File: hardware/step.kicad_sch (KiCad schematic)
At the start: 51 parts, among them J101 WAGO 2065-100, J102 WAGO 2065-100, J103 Cortex, SW101 SKSG, SW102 SKSG, U101 ATSAMD51J, U102 TPS78433QWDRBRQ1, Y101 32k768

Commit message: Refresh
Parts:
- C107, C108: Manufacturer YAGEO -> TDK; Mouser 603-CC603JRNPO9BN180 -> 810-CGA3E2C0G1H180J; Product CC0603JRNPO9BN180 -> CGA3E2C0G1H180J080AA
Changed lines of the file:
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@@
 	(title_block
 		(title "V2 step")
-		(date "2026-03-02")
+		(date "2026-03-11")
 		(rev "2025-11-30")
 		(company "Versio Duo")
@@
 			)
 		)
-		(property "Description" "Unpolarized capacitor, small symbol"
+		(property "Description" ""
 			(at 109.22 37.592 0)
 			(effects
@@
 		(at 223.52 165.1 0)
 		(unit 1)
-		(exclude_from_sim yes)
+		(exclude_from_sim no)
 		(in_bom no)
 		(on_board yes)
@@
 			)
 		)
+		(property "Sim.Enable" "0"
+			(at 223.52 165.1 0)
+			(effects
+				(font
+					(size 1.27 1.27)
+				)
+				(hide yes)
+			)
+		)
 		(instances
 			(project ""
@@
 			)
 		)
-		(property "Description" "Push button switch, generic, two pins"
+		(property "Description" "Push button"
 			(at 118.11 157.48 0)
 			(effects
@@
 			)
 		)
-		(property "Description" "Light emitting diode, small symbol"
+		(property "Description" ""
 			(at 128.27 86.36 0)
 			(effects
@@
 			)
 		)
-		(property "Description" "Resistor, small symbol"
+		(property "Description" ""
 			(at 243.84 80.772 0)
 			(effects
@@
 		(at 190.5 152.4 0)
 		(unit 1)
-		(exclude_from_sim yes)
+		(exclude_from_sim no)
 		(in_bom no)
 		(on_board yes)
@@
 			)
 		)
+		(property "Sim.Enable" "0"
+			(at 190.5 152.4 0)
+			(effects
+				(font
+					(size 1.27 1.27)
+				)
+				(hide yes)
+			)
+		)
 		(instances
 			(project "pulse"
@@
 			)
 		)
-		(property "Description" "Unpolarized capacitor, small symbol"
+		(property "Description" ""
 			(at 58.42 182.372 0)
 			(effects
@@
 		(at 223.52 152.4 0)
 		(unit 1)
-		(exclude_from_sim yes)
+		(exclude_from_sim no)
 		(in_bom no)
 		(on_board yes)
@@
 			)
 		)
+		(property "Sim.Enable" "0"
+			(at 223.52 152.4 0)
+			(effects
+				(font
+					(size 1.27 1.27)
+				)
+				(hide yes)
+			)
+		)
 		(instances
 			(project "pulse"
@@
 			)
 		)
-		(property "Description" "Unpolarized capacitor, small symbol"
+		(property "Description" ""
 			(at 119.38 37.592 0)
 			(effects
@@
 			)
 		)
-		(property "Description" "Resistor, small symbol"
+		(property "Description" ""
 			(at 268.732 66.04 0)
 			(effects
@@
 		(at 190.5 160.02 0)
 		(unit 1)
-		(exclude_from_sim yes)
+		(exclude_from_sim no)
 		(in_bom no)
 		(on_board yes)
@@
 			)
 		)
+		(property "Sim.Enable" "0"
+			(at 190.5 160.02 0)
+			(effects
+				(font
+					(size 1.27 1.27)
+				)
+				(hide yes)
+			)
+		)
 		(instances
 			(project "pulse"
@@
 			)
 		)
-		(property "Description" "Unpolarized capacitor, small symbol"
+		(property "Description" ""
 			(at 33.02 182.372 0)
 			(effects
@@
 			)
 		)
-		(property "Description" "Two pin crystal, small symbol"
+		(property "Description" ""
 			(at 24.13 43.18 0)
 			(effects
@@
 			)
 		)
-		(property "Description" "Unpolarized capacitor, small symbol"
+		(property "Description" ""
 			(at 26.67 60.452 0)
 			(effects
@@
 			)
 		)
-		(property "Mouser" "603-CC603JRNPO9BN180"
+		(property "Mouser" "810-CGA3E2C0G1H180J"
 			(at 26.67 64.516 0)
 			(effects
@@
 			)
 		)
-		(property "Product" "CC0603JRNPO9BN180"
+		(property "Product" "CGA3E2C0G1H180J080AA"
 			(at 26.67 67.564 0)
 			(effects
@@
 			)
 		)
-		(property "Manufacturer" "YAGEO"
+		(property "Manufacturer" "TDK"
 			(at 26.67 64.77 0)
 			(effects
@@
 			)
 		)
-		(property "Description" "Unpolarized capacitor, small symbol"
+		(property "Description" ""
 			(at 57.15 37.592 0)
 			(effects
@@
 			)
 		)
-		(property "Description" "Unpolarized capacitor, small symbol"
+		(property "Description" ""
 			(at 21.59 60.452 0)
 			(effects
@@
 			)
 		)
-		(property "Mouser" "603-CC603JRNPO9BN180"
+		(property "Mouser" "810-CGA3E2C0G1H180J"
 			(at 21.59 64.516 0)
 			(effects
@@
 			)
 		)
-		(property "Product" "CC0603JRNPO9BN180"
+		(property "Product" "CGA3E2C0G1H180J080AA"
 			(at 21.59 67.564 0)
 			(effects
@@
 			)
 		)
-		(property "Manufacturer" "YAGEO"
+		(property "Manufacturer" "TDK"
 			(at 21.59 64.77 0)
 			(effects
@@
 		(at 157.48 160.02 0)
 		(unit 1)
-		(exclude_from_sim yes)
+		(exclude_from_sim no)
 		(in_bom no)
 		(on_board yes)
@@
 			)
 		)
+		(property "Sim.Enable" "0"
+			(at 157.48 160.02 0)
+			(effects
+				(font
+					(size 1.27 1.27)
+				)
+				(hide yes)
+			)
+		)
 		(instances
 			(project ""
@@
 			)
 		)
-		(property "Description" "Resistor, small symbol"
+		(property "Description" ""
 			(at 149.352 86.36 0)
 			(effects
@@
 			)
 		)
-		(property "Description" "Unpolarized capacitor, small symbol"
+		(property "Description" ""
 			(at 261.62 82.042 0)
 			(effects
@@
 			)
 		)
-		(property "Description" "Unpolarized capacitor, small symbol"
+		(property "Description" ""
 			(at 99.06 37.592 0)
 			(effects
@@
 			)
 		)
-		(property "Description" "Unpolarized capacitor, small symbol"
+		(property "Description" ""
 			(at 78.74 37.592 0)
 			(effects
@@
 		(at 223.52 158.75 0)
 		(unit 1)
-		(exclude_from_sim yes)
+		(exclude_from_sim no)
 		(in_bom no)
 		(on_board yes)
@@
 			)
 		)
+		(property "Sim.Enable" "0"
+			(at 223.52 158.75 0)
+			(effects
+				(font
+					(size 1.27 1.27)
+				)
+				(hide yes)
+			)
+		)
 		(instances
 			(project ""
@@
 			)
 		)
-		(property "Description" "Push button switch, generic, two pins"
+		(property "Description" "Push button"
 			(at 129.54 73.152 0)
 			(effects
@@
 			)
 		)
-		(property "Description" "Unpolarized capacitor, small symbol"
+		(property "Description" ""
 			(at 88.9 37.592 0)
 			(effects
@@
 			)
 		)
-		(property "Description" "Resistor, small symbol"
+		(property "Description" ""
 			(at 243.84 75.692 0)
 			(effects
@@
 			)
 		)
-		(property "Description" "Resistor, small symbol"
+		(property "Description" ""
 			(at 62.992 121.92 0)
 			(effects
@@
 		(at 190.5 168.91 0)
 		(unit 1)
-		(exclude_from_sim yes)
+		(exclude_from_sim no)
 		(in_bom no)
 		(on_board yes)
@@
 			(at 190.5 168.91 0)
 			(effects
+				(font
+					(size 1.27 1.27)
+				)
+				(hide yes)
+			)
+		)
+		(property "Sim.Enable" "0"
+			(at 190.5 168.91 0)
+			(effects

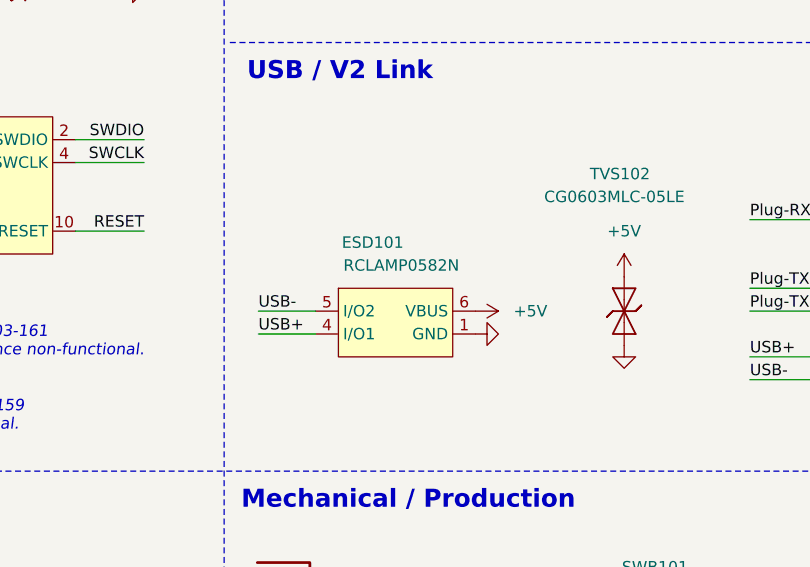
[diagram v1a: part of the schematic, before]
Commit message: Update ESD suppressor
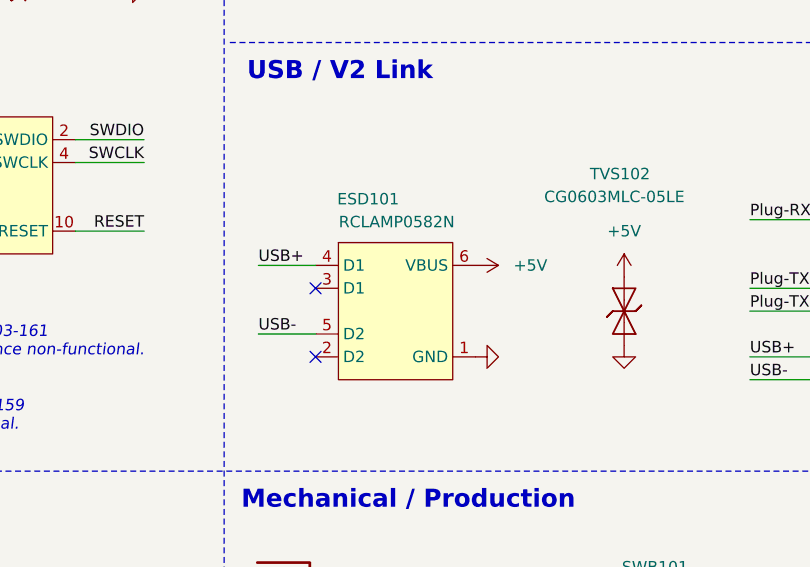
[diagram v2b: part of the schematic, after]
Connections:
- no-connect marks 23 -> 25
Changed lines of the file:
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@@
 	(title_block
 		(title "V2 step")
-		(date "2026-03-11")
+		(date "2026-03-14")
 		(rev "2025-11-30")
 		(company "Versio Duo")
@@
 	)
 	(no_connect
+		(at 161.29 127)
+	)
+	(no_connect
 		(at 133.35 180.34)
 	)
 	(no_connect
+		(at 161.29 119.38)
+	)
+	(no_connect
 		(at 53.34 55.88)
 	)
@@
 	(wire
 		(pts
+			(xy 154.94 116.84) (xy 161.29 116.84)
+		)
+		(stroke
+			(width 0)
+			(type default)
+		)
+	)
+	(wire
+		(pts
 			(xy 72.39 21.59) (xy 72.39 33.02)
 		)
@@
 	(wire
 		(pts
-			(xy 154.94 124.46) (xy 161.29 124.46)
-		)
-		(stroke
-			(width 0)
-			(type default)
-		)
-	)
-	(wire
-		(pts
 			(xy 118.11 173.99) (xy 133.35 173.99)
 		)
@@
 	(wire
 		(pts
-			(xy 154.94 121.92) (xy 161.29 121.92)
+			(xy 154.94 124.46) (xy 161.29 124.46)
 		)
 		(stroke
@@
 		)
 	)
+	(label "USB+"
+		(at 154.94 116.84 0)
+		(effects
+			(font
+				(size 1.27 1.27)
+			)
+			(justify left bottom)
+		)
+	)
 	(label "LED1"
 		(at 160.02 48.26 0)
@@
 	)
 	(label "USB-"
-		(at 154.94 121.92 0)
+		(at 154.94 124.46 0)
 		(effects
 			(font
@@
 		)
 	)
-	(label "USB+"
-		(at 154.94 124.46 0)
-		(effects
-			(font
-				(size 1.27 1.27)
-			)
-			(justify left bottom)
-		)
-	)
 	(label "Socket-TX"
 		(at 247.65 123.19 0)
@@
 	(symbol
 		(lib_id "V2_power:+5V")
-		(at 179.07 121.92 270)
+		(at 179.07 116.84 270)
 		(unit 1)
 		(exclude_from_sim no)
@@
 		(dnp no)
 		(property "Reference" "#PWR124"
-			(at 175.26 121.92 0)
+			(at 175.26 116.84 0)
 			(effects
 				(font
@@
 		)
 		(property "Value" "+5V"
-			(at 185.166 121.92 90)
+			(at 185.166 116.84 90)
 			(effects
 				(font
@@
 		)
 		(property "Footprint" ""
-			(at 179.07 121.92 0)
+			(at 179.07 116.84 0)
 			(effects
 				(font
@@
 		)
 		(property "Datasheet" ""
-			(at 179.07 121.92 0)
+			(at 179.07 116.84 0)
 			(effects
 				(font
@@
 		)
 		(property "Description" ""
-			(at 179.07 121.92 0)
+			(at 179.07 116.84 0)
 			(effects
 				(font
@@
 		(dnp no)
 		(property "Reference" "ESD101"
-			(at 167.64 114.3 0)
+			(at 167.132 109.474 0)
 			(effects
 				(font
@@
 		)
 		(property "Value" "RCLAMP0582N"
-			(at 170.815 116.84 0)
+			(at 170.307 112.014 0)
 			(effects
 				(font
@@
 	(symbol
 		(lib_id "V2_power:GND")
-		(at 179.07 124.46 90)
+		(at 179.07 127 90)
 		(unit 1)
 		(exclude_from_sim no)
@@
 		(dnp no)
 		(property "Reference" "#PWR125"
-			(at 185.42 124.46 0)
+			(at 185.42 127 0)
 			(effects
 				(font
@@
 		)
 		(property "Value" "GND"
-			(at 184.15 124.46 90)
+			(at 184.15 127 90)
 			(effects
 				(font
@@
 		)
 		(property "Footprint" ""
-			(at 179.07 124.46 0)
+			(at 179.07 127 0)
 			(effects
 				(font
@@
 		)
 		(property "Datasheet" ""
-			(at 179.07 124.46 0)
+			(at 179.07 127 0)
 			(effects
 				(font
@@
 		)
 		(property "Description" ""
-			(at 179.07 124.46 0)
+			(at 179.07 127 0)
 			(effects
 				(font

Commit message: KiCad 10
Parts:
- INFO102: value ~ -> (none)

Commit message: Refresh
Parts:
- C107, C108: Rating (none) -> 50V
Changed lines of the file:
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@@
 		(unit 1)
 		(body_style 1)
-		(exclude_from_sim no)
+		(exclude_from_sim yes)
 		(in_bom no)
 		(on_board yes)
@@
 		(unit 1)
 		(body_style 1)
-		(exclude_from_sim no)
-		(in_bom yes)
-		(on_board yes)
+		(exclude_from_sim yes)
+		(in_bom no)
+		(on_board no)
 		(in_pos_files yes)
 		(dnp no)
@@
 		(unit 1)
 		(body_style 1)
-		(exclude_from_sim no)
-		(in_bom yes)
-		(on_board yes)
+		(exclude_from_sim yes)
+		(in_bom no)
+		(on_board no)
 		(in_pos_files yes)
 		(dnp no)
@@
 		(unit 1)
 		(body_style 1)
-		(exclude_from_sim no)
+		(exclude_from_sim yes)
 		(in_bom no)
 		(on_board yes)
@@
 		(unit 1)
 		(body_style 1)
-		(exclude_from_sim no)
-		(in_bom yes)
-		(on_board yes)
+		(exclude_from_sim yes)
+		(in_bom no)
+		(on_board no)
 		(in_pos_files yes)
 		(dnp no)
@@
 		(unit 1)
 		(body_style 1)
-		(exclude_from_sim no)
+		(exclude_from_sim yes)
 		(in_bom no)
 		(on_board yes)
@@
 		(unit 1)
 		(body_style 1)
-		(exclude_from_sim no)
-		(in_bom yes)
-		(on_board yes)
+		(exclude_from_sim yes)
+		(in_bom no)
+		(on_board no)
 		(in_pos_files yes)
 		(dnp no)
@@
 		(unit 1)
 		(body_style 1)
-		(exclude_from_sim no)
+		(exclude_from_sim yes)
 		(in_bom no)
 		(on_board yes)
@@
 			)
 		)
+		(property "Rating" "50V"
+			(at 26.67 72.39 0)
+			(hide yes)
+			(show_name no)
+			(do_not_autoplace no)
+			(effects
+				(font
+					(size 1.27 1.27)
+				)
+			)
+		)
 		(pin "1"
 		)
@@
 			)
 		)
+		(property "Rating" "50V"
+			(at 21.59 72.39 0)
+			(hide yes)
+			(show_name no)
+			(do_not_autoplace no)
+			(effects
+				(font
+					(size 1.27 1.27)
+				)
+			)
+		)
 		(pin "1"
 		)
@@
 		(unit 1)
 		(body_style 1)
-		(exclude_from_sim no)
+		(exclude_from_sim yes)
 		(in_bom no)
 		(on_board yes)
@@
 		(unit 1)
 		(body_style 1)
-		(exclude_from_sim no)
+		(exclude_from_sim yes)
 		(in_bom no)
 		(on_board yes)
@@
 		(unit 1)
 		(body_style 1)
-		(exclude_from_sim no)
+		(exclude_from_sim yes)
 		(in_bom no)
 		(on_board yes)

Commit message: Update
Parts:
- C101, C102, C103, C104, C105, C106, C107, C108, C109, C110, C111: Id (none) -> Capacitor:${SYMBOL_NAME}
- D101: Id (none) -> LED:${SYMBOL_NAME}; Rating (none) -> 605nm
- D102, D103: Id (none) -> LED:${SYMBOL_NAME}; Rating (none) -> 15mA
- ESD101: Id (none) -> ESD:${SYMBOL_NAME}
- J101, J102: Id (none) -> WAGO:${SYMBOL_NAME}
- R101, R102, R103, R104, R105: Id (none) -> Resistor:${SYMBOL_NAME}
- SW101, SW102: Id (none) -> Button:${SYMBOL_NAME}; Rating (none) -> 1.6N
- TVS101, TVS102: Id (none) -> Diode:${SYMBOL_NAME}
- U101: Id (none) -> MCU:${SYMBOL_NAME}
- U102: Id (none) -> LDO:${SYMBOL_NAME}; Rating (none) -> 300mA
- Y101: Id (none) -> Crystal:${SYMBOL_NAME}; Rating (none) -> 10ppm

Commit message: Update
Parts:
- ESD101: Rating (none) -> 20kV
- J101, J102: Rating (none) -> 9A
- U101: Rating (none) -> Cortex-M4F
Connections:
- net VDDCORE renamed +VCORE
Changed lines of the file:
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@@
 	(title_block
 		(title "V2 step")
-		(date "2026-04-11")
+		(date "2026-04-14")
 		(rev "2026-02-10")
 		(company "Versio Duo")
@@
 		)
 	)
-	(label "VDDCORE"
+	(label "+VCORE"
 		(at 58.42 21.59 0)
 		(effects
@@
 			)
 		)
+		(property "Rating" "20kV"
+			(at 170.18 151.13 0)
+			(hide yes)
+			(show_name no)
+			(do_not_autoplace no)
+			(effects
+				(font
+					(size 1.27 1.27)
+				)
+			)
+		)
 		(pin "1"
 		)
@@
 			)
 		)
+		(property "Rating" "Cortex-M4F"
+			(at 69.85 161.29 0)
+			(hide yes)
+			(show_name no)
+			(do_not_autoplace no)
+			(effects
+				(font
+					(size 1.27 1.27)
+				)
+			)
+		)
 		(pin "64"
 			(alternate "GPIOIN")
@@
 			)
 		)
+		(property "Rating" "9A"
+			(at 245.11 57.15 0)
+			(hide yes)
+			(show_name no)
+			(do_not_autoplace no)
+			(effects
+				(font
+					(size 1.27 1.27)
+				)
+			)
+		)
 		(pin "1"
 		)
@@
 			(hide yes)
 			(show_name no)
+			(do_not_autoplace no)
+			(effects
+				(font
+					(size 1.27 1.27)
+				)
+			)
+		)
+		(property "Rating" "9A"
+			(at 245.11 49.53 0)
+			(hide yes)
+			(show_name no)

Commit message: Good Bye Imperial
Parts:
- C101: renamed from C107; footprint V2_Capacitor_SMD:C_0603 -> V2_Capacitor_SMD:C_1608; symbol V2_Capacitor:0603_18p -> V2_Capacitor:1608_18p
- C102: renamed from C108; footprint V2_Capacitor_SMD:C_0603 -> V2_Capacitor_SMD:C_1608; symbol V2_Capacitor:0603_18p -> V2_Capacitor:1608_18p
- C103: renamed from C110; footprint V2_Capacitor_SMD:C_0805 -> V2_Capacitor_SMD:C_2012; symbol V2_Capacitor:0805_10u -> V2_Capacitor:2012_10u
- C104: renamed from C101; footprint V2_Capacitor_SMD:C_0603 -> V2_Capacitor_SMD:C_1608; symbol V2_Capacitor:0603_10u -> V2_Capacitor:1608_10u
- C105: renamed from C111; footprint V2_Capacitor_SMD:C_0805 -> V2_Capacitor_SMD:C_2012; symbol V2_Capacitor:0805_10u -> V2_Capacitor:2012_10u
- C106: renamed from C102; footprint V2_Capacitor_SMD:C_0603 -> V2_Capacitor_SMD:C_1608; symbol V2_Capacitor:0603_0u1 -> V2_Capacitor:1608_0u1
- C107: renamed from C103; footprint V2_Capacitor_SMD:C_0603 -> V2_Capacitor_SMD:C_1608; symbol V2_Capacitor:0603_0u1 -> V2_Capacitor:1608_0u1
- C108: renamed from C104; footprint V2_Capacitor_SMD:C_0603 -> V2_Capacitor_SMD:C_1608; symbol V2_Capacitor:0603_0u1 -> V2_Capacitor:1608_0u1
- C109: renamed from C105; footprint V2_Capacitor_SMD:C_0603 -> V2_Capacitor_SMD:C_1608; symbol V2_Capacitor:0603_0u1 -> V2_Capacitor:1608_0u1
- C110: renamed from C106; footprint V2_Capacitor_SMD:C_0603 -> V2_Capacitor_SMD:C_1608; symbol V2_Capacitor:0603_0u1 -> V2_Capacitor:1608_0u1
- C111: renamed from C109; footprint V2_Capacitor_SMD:C_0603 -> V2_Capacitor_SMD:C_1608; symbol V2_Capacitor:0603_0u1 -> V2_Capacitor:1608_0u1
- D103: renamed from D101; footprint V2_LED:LED_0603 -> V2_LED:LED_1608; symbol V2_LED:0603_Orange -> V2_LED:1608_Orange
- R101: renamed from R105; footprint V2_Resistor_SMD:R_0603 -> V2_Resistor_SMD:R_1608; symbol V2_Resistor:0603_100k -> V2_Resistor:1608_100k
- R102: renamed from R104; footprint V2_Resistor_SMD:R_0603 -> V2_Resistor_SMD:R_1608; symbol V2_Resistor:0603_330R -> V2_Resistor:1608_330R
- R103: renamed from R101; footprint V2_Resistor_SMD:R_0603 -> V2_Resistor_SMD:R_1608; symbol V2_Resistor:0603_100k -> V2_Resistor:1608_100k
- R104: renamed from R103; footprint V2_Resistor_SMD:R_0603 -> V2_Resistor_SMD:R_1608; symbol V2_Resistor:0603_10k -> V2_Resistor:1608_10k
- R105: renamed from R102; footprint V2_Resistor_SMD:R_0603 -> V2_Resistor_SMD:R_1608; symbol V2_Resistor:0603_10k -> V2_Resistor:1608_10k
- TVS101: renamed from TVS102; footprint V2_Diode_SMD:D_0603 -> V2_Diode_SMD:D_1608
- renumbered D102 to D101, D103 to D102, H103 to H102, H105 to H103, H107 to H104, H108 to H105, H102 to H106, H104 to H107, H106 to H108, ICON105 to ICON101, ICON104 to ICON102, ICON101 to ICON103, ICON102 to ICON104, ICON103 to ICON105, INFO102 to INFO101, INFO101 to INFO102, J103 to J101, J101 to J102, J102 to J103, SW102 to SW101, SW101 to SW102, TVS101 to TVS102, U102 to U101, U101 to U102
